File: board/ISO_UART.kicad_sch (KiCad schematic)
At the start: 8 parts, among them J1 Conn_01x04, U2 TCMT1100, U3 TCMT1100

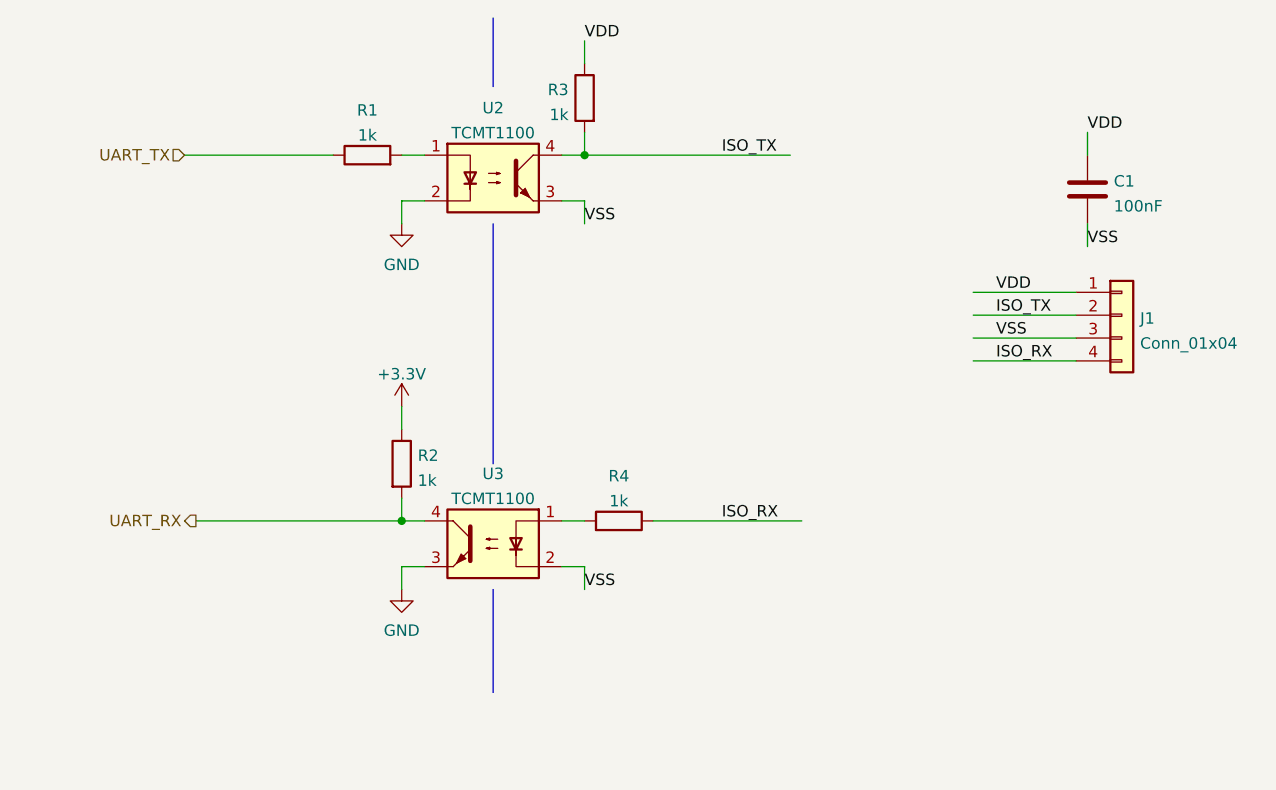
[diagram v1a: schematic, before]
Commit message: updating optocouplers
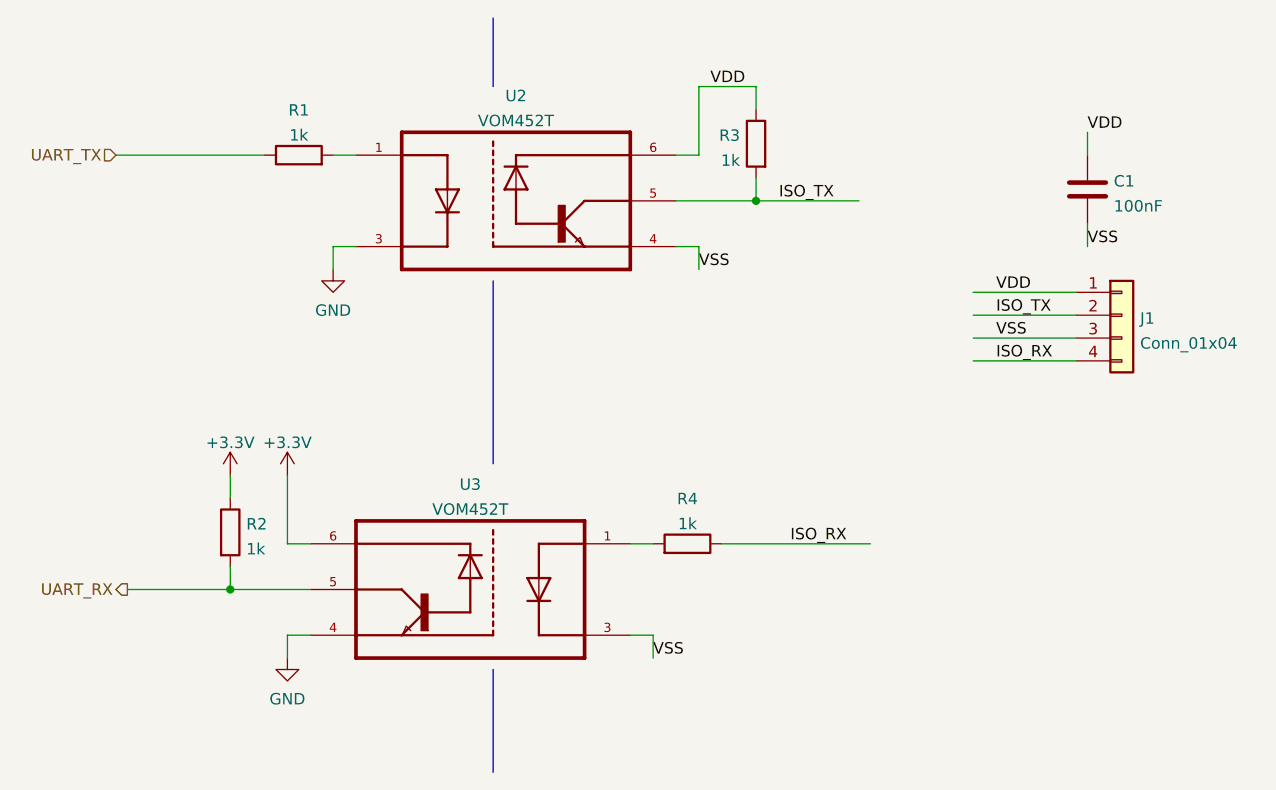
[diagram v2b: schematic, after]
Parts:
- removed U2, U3: TCMT1100, Package_SO:SOP-4_4.4x2.6mm_P1.27mm, symbol Isolator:TCMT1100
- added U2, U3: VOM452T, SOIC127P700X230-5N, symbol VOM452T:VOM452T
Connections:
- net +3V3: now also U3.6
- net GND: now also U2.3, U3.4
- net ISO_TX: now also U2.5
- net UART_RX: now also U3.5
- net VDD: now also U2.6
- net VSS: now also U2.4, U3.3
- net at R4.2: now also U3.1
- net at R1.2: now also U2.1
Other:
- moved on the sheet: R1, R2, R3, R4

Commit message: Updating pdf
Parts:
- U2, U3: MFG PN (none) -> VOM452T
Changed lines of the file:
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@@
       (effects (font (size 1.27 1.27)) (justify left bottom) hide)
+    )
+    (property "MFG PN" "VOM452T" (id 5) (at 139.7 104.14 0)
+      (effects (font (size 1.27 1.27)) hide)
     )
     (pin "1")
@@
       (effects (font (size 1.27 1.27)) (justify left bottom) hide)
     )
+    (property "MFG PN" "VOM452T" (id 5) (at 144.78 60.96 0)
+      (effects (font (size 1.27 1.27)) hide)
+    )
     (pin "1")
     (pin "3")
@@
   (symbol (lib_id "power:+3.3V") (at 119.38 91.44 0)
     (in_bom yes) (on_board yes) (fields_autoplaced)
-    (property "Reference" "#PWR?" (id 0) (at 119.38 95.25 0)
+    (property "Reference" "#PWR026" (id 0) (at 119.38 95.25 0)
       (effects (font (size 1.27 1.27)) hide)
     )

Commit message: Adding LCSC part numbers
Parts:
- C1: LCSC (none) -> C14663
- J1: LCSC (none) -> C157926
- R1, R2, R3, R4: LCSC (none) -> C21190
- U2, U3: LCSC (none) -> C141603
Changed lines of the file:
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@@
+      (effects (font (size 1.27 1.27)) hide)
+    )
+    (property "LCSC" "C141603" (id 6) (at 139.7 104.14 0)
       (effects (font (size 1.27 1.27)) hide)
     )
@@
       (effects (font (size 1.27 1.27)) hide)
     )
+    (property "LCSC" "C21190" (id 4) (at 163.83 99.06 0)
+      (effects (font (size 1.27 1.27)) hide)
+    )
     (pin "1")
     (pin "2")
@@
     )
     (property "Datasheet" "~" (id 3) (at 113.03 97.79 0)
+      (effects (font (size 1.27 1.27)) hide)
+    )
+    (property "LCSC" "C21190" (id 4) (at 113.03 97.79 0)
       (effects (font (size 1.27 1.27)) hide)
     )
@@
       (effects (font (size 1.27 1.27)) hide)
     )
+    (property "LCSC" "C14663" (id 4) (at 208.28 59.69 0)
+      (effects (font (size 1.27 1.27)) hide)
+    )
     (pin "1")
     (pin "2")
@@
     )
     (property "Datasheet" "~" (id 3) (at 171.45 54.61 0)
+      (effects (font (size 1.27 1.27)) hide)
+    )
+    (property "LCSC" "C21190" (id 4) (at 171.45 54.61 0)
       (effects (font (size 1.27 1.27)) hide)
     )
@@
       (effects (font (size 1.27 1.27)) hide)
     )
+    (property "LCSC" "C21190" (id 4) (at 120.65 55.88 0)
+      (effects (font (size 1.27 1.27)) hide)
+    )
     (pin "1")
     (pin "2")
@@
     )
     (property "MFG PN" "VOM452T" (id 5) (at 144.78 60.96 0)
+      (effects (font (size 1.27 1.27)) hide)
+    )
+    (property "LCSC" "C141603" (id 6) (at 144.78 60.96 0)
       (effects (font (size 1.27 1.27)) hide)
     )
@@
       (effects (font (size 1.27 1.27)) hide)
     )
+    (property "LCSC" "C157926" (id 4) (at 212.09 73.66 0)
+      (effects (font (size 1.27 1.27)) hide)
+    )
